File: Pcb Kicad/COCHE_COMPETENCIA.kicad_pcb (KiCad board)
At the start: 2 copper layers, 95 x 62 mm, 29 parts, among them J1 BAT, J2 SWITCH, J4 M1, J5 M2, J6 SENSORES, SW1 SW_Push, SW2 SW_Push, U1 L7805, U2 ESP32-DEVKIT-V1, U3 DRV8833, U4 DRV8833

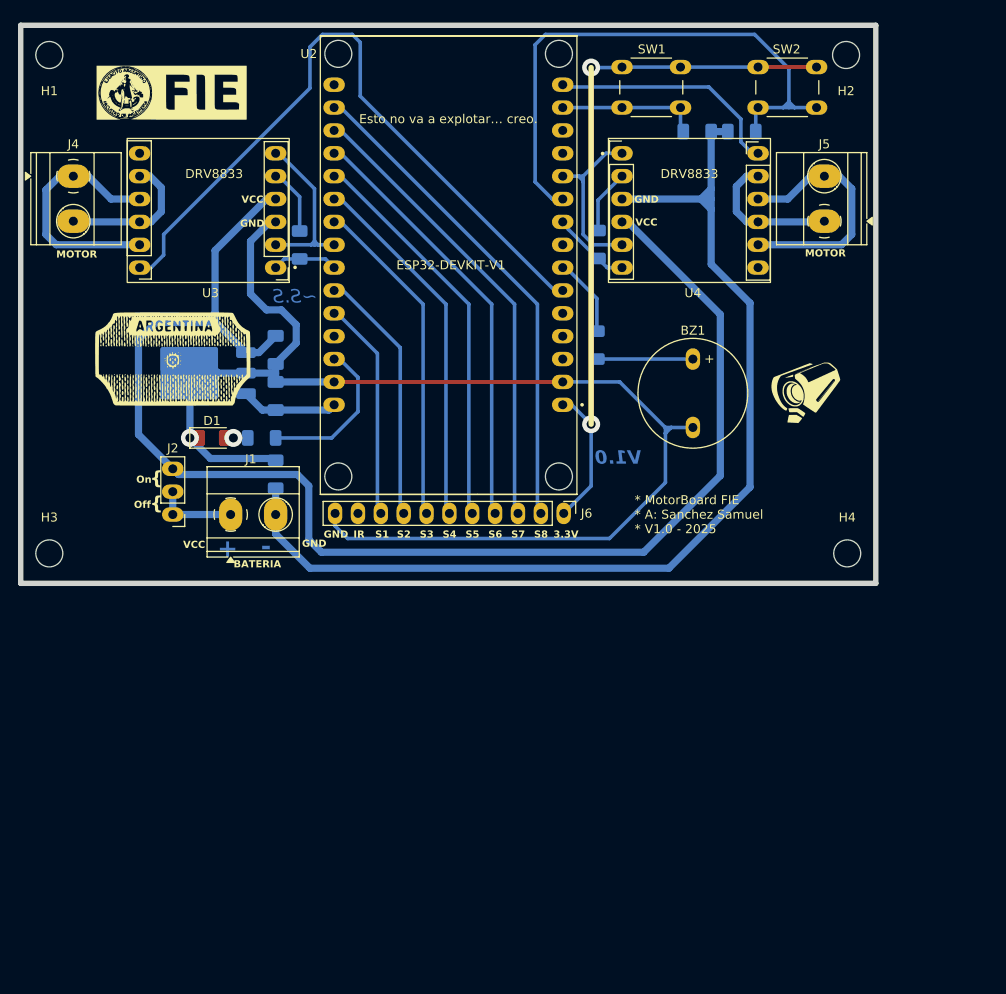
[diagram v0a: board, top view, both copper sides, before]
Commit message: V1.1 - Correccion de bocina y programas de motores.
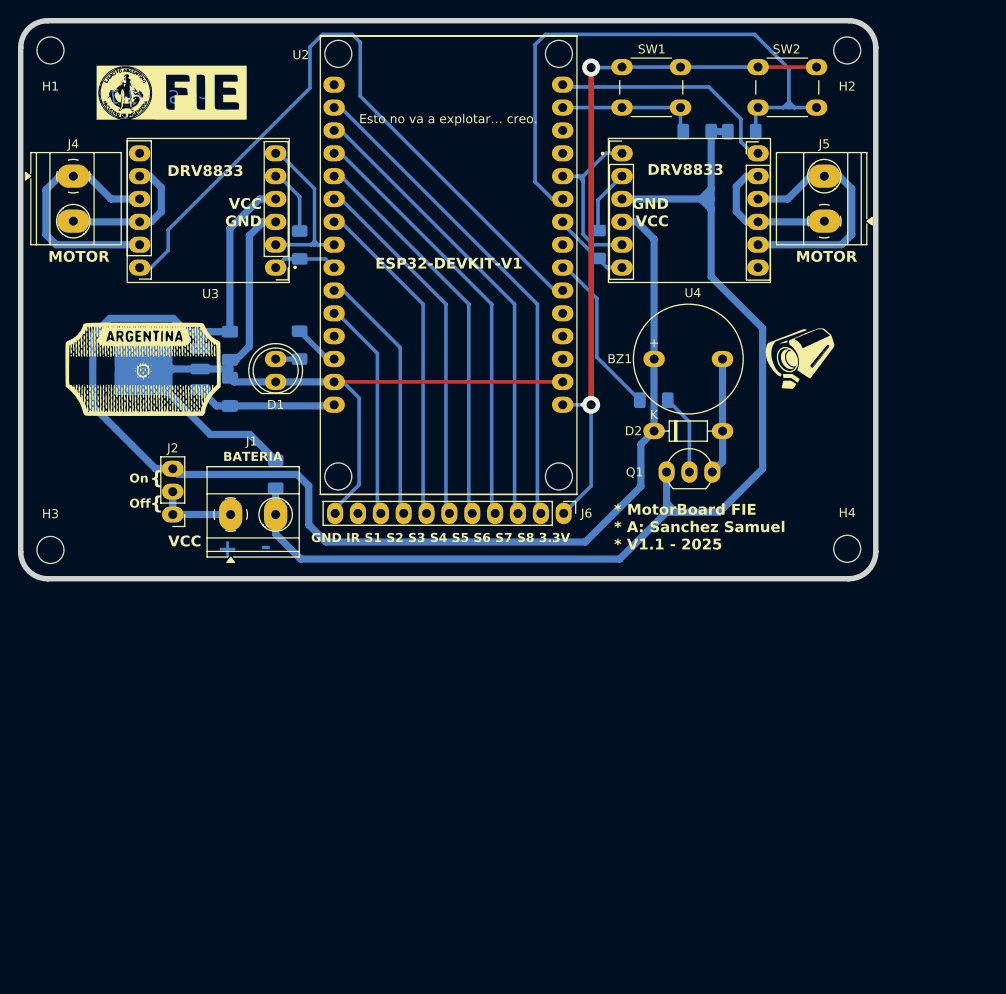
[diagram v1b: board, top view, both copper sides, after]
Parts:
- added D2: 1N4148, Diode_THT:D_DO-35_SOD27_P7.62mm_Horizontal, F.Cu at (168.0, 69.8)
- added Q1: 2N3904, Package_TO_SOT_THT:TO-92_Inline_Wide, F.Cu at (169.4, 74.4)
- D1: footprint LED_SMD:LED_1206_3216Metric_Pad1.42x1.75mm_HandSolder -> LED_THT:LED_D5.0mm
- R7: value 0 -> 1k
- moved R4 11.1 mm to (128.7, 60.3), turned to -90 degrees
- moved D1 9.42 mm to (126.0, 64.4), turned to 90 degrees
- moved R7 8.80 mm to (168.0, 66.4), turned to 0 degrees
- moved C1 5.10 mm to (120.9, 60.4)
- moved C2 5.10 mm to (120.9, 65.5)
- moved U1 5.10 mm to (112.6, 63.0)
- moved BZ1 4.31 mm to (168.0, 61.8), turned to 0 degrees
- moved G*** 3.85 mm to (184.2, 61.8)
- moved G*** 3.49 mm to (111.3, 63.0)
- moved H1 0.52 mm to (101.0, 27.6)
- moved H2 0.52 mm to (189.5, 27.6)
- moved H4 0.51 mm to (189.5, 82.9)
- moved H3 0.40 mm to (101.0, 83.1)
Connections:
- BZ1 pad 1: Net-(BZ1-+) -> VCC
- BZ1 pad 2: GND -> Net-(BZ1--)
- R7 pad 2: Net-(BZ1-+) -> Net-(Q1-B)
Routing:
- net GND: track 269.8 -> 230.0 mm, vias 1 -> 0
- net Net-(BZ1--): track 0.00 -> 13.4 mm
- net /LED_LARGADA: track 17.7 -> 5.89 mm
- net Net-(BZ1-+): track 10.7 -> 0.00 mm
- net /BUZZER: track 8.85 -> 18.5 mm
- net Net-(Q1-B): track 0.00 -> 8.98 mm
- net VCC: track 157.4 -> 151.5 mm
- net +5V: track 10.8 -> 16.5 mm
- net +3.3V: track 80.6 -> 79.7 mm
- net Net-(D1-A): track 2.49 -> 2.67 mm, vias 1 -> 0
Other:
- outline, holes or cut-outs redrawn
- board text added: "* MotorBoard FIE * A: Sanchez Samuel * V1.1 - 2025"
- board text added: "GND IR S1 S2 S3 S4 S5 S6 S7 S8 3.3V"
- board text added: "GND VCC"
- board text added: "VCC GND"
- board text added: "~S.S - V1.1"
- board text removed: "* MotorBoard FIE * A: Sanchez Samuel * V1.0 - 2025"
- board text removed: "3.3V"
- board text removed: "GND"
- board text removed: "IR"
- board text removed: "S1"
- board text removed: "S2"
- board text removed: "S3"
- board text removed: "S4"
- board text removed: "S5"
- board text removed: "S6"
- board text removed: "S7"
- board text removed: "S8"
- board text removed: "V1.0"
- board text removed: "~S.S"

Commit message: V1.1 - Programa de Buzzer + Modulo Drv8833
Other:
- board text added: "ANTENA"
- board text added: "USB"
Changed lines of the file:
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@@
+		)
+	)
+	(gr_text "ANTENA"
+		(at 150.241 30.607 0)
+		(layer "F.SilkS")
+		(effects
+			(font
+				(size 2 2)
+				(thickness 0.45)
+				(bold yes)
+			)
+			(justify right bottom)
+		)
+	)
+	(gr_text "USB"
+		(at 147.193 72.39 0)
+		(layer "F.SilkS")
+		(effects
+			(font
+				(size 1.5 1.5)
+				(thickness 0.375)
+				(bold yes)
+			)
+			(justify right bottom)
 		)
 	)

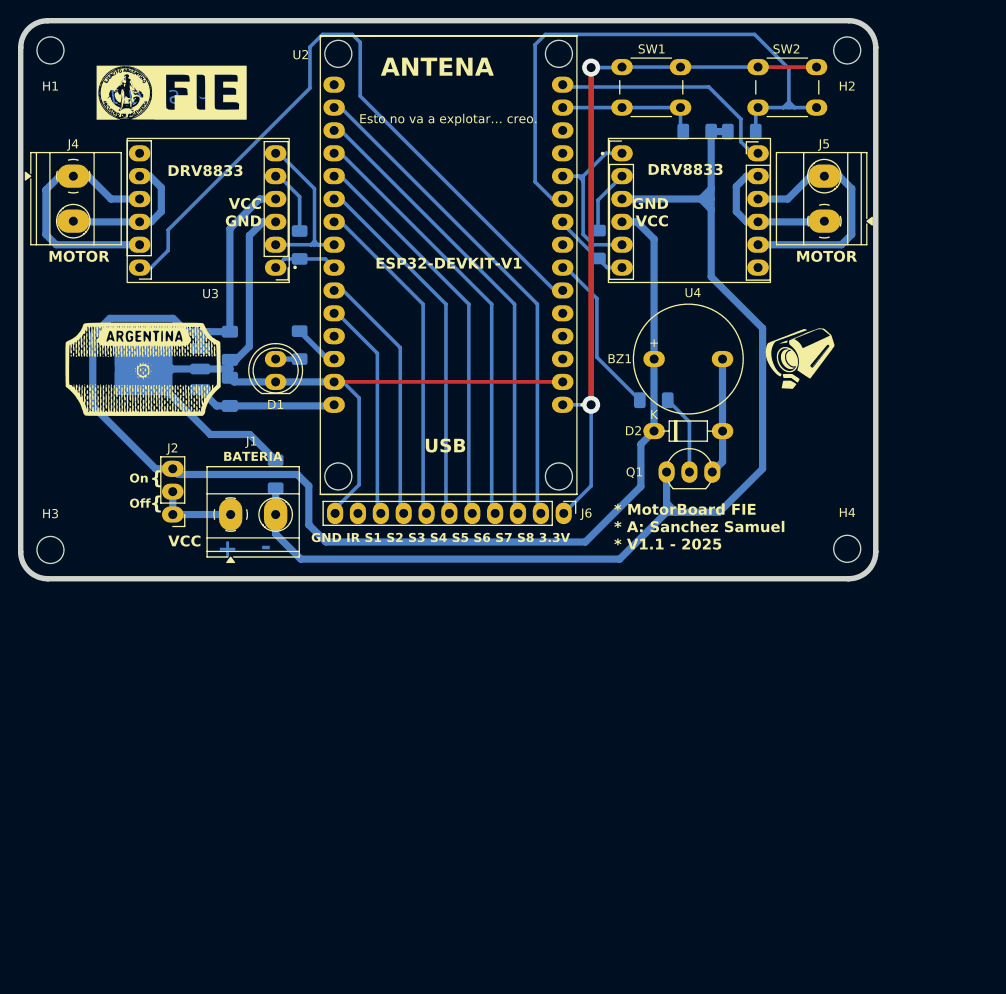
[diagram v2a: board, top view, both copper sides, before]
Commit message: V1.2 - Mejoras de PCB: alimentacion, bocina y borneras.
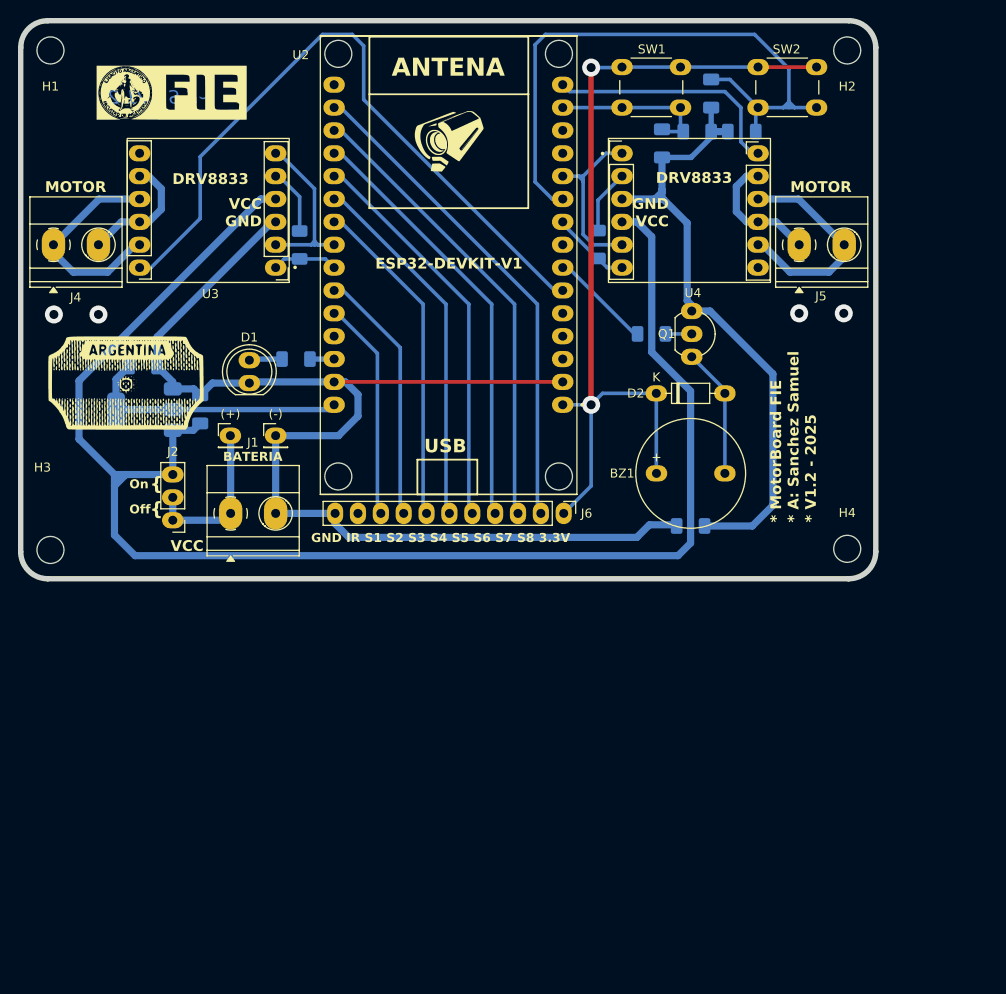
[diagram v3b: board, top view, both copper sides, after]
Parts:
- removed U1: L7805, Package_TO_SOT_SMD:TO-252-3_TabPin2
- added (+): TestPoint, Connector_PinHeader_2.54mm:PinHeader_1x01_P2.54mm_Vertical, F.Cu at (121.0, 70.4)
- added (-): TestPoint, Connector_PinHeader_2.54mm:PinHeader_1x01_P2.54mm_Vertical, F.Cu at (126.0, 70.4)
- added C3: 0.1u, Capacitor_SMD:C_1206_3216Metric_Pad1.33x1.80mm_HandSolder, B.Cu at (168.9, 37.9)
- added C4: 0.1u, Capacitor_SMD:C_1206_3216Metric_Pad1.33x1.80mm_HandSolder, B.Cu at (174.4, 32.3)
- added U5: AMS1117, Package_TO_SOT_SMD:SOT-223-3_TabPin2, B.Cu at (111.4, 67.5)
- moved R1 46.5 mm to (172.1, 80.4), turned to 180 degrees
- moved G*** 45.9 mm to (145.2, 37.7)
- moved Q1 18.1 mm to (172.2, 56.5), turned to -90 degrees
- moved BZ1 12.7 mm to (168.3, 74.5)
- moved C2 10.1 mm to (111.3, 62.6), turned to 0 degrees
- moved J4 7.93 mm to (101.3, 49.1), turned to 0 degrees
- moved C1 7.80 mm to (117.6, 67.4), turned to 90 degrees
- moved R7 7.37 mm to (167.7, 59.1)
- moved D2 4.20 mm to (168.3, 65.7)
- moved J5 3.83 mm to (184.2, 49.1), turned to 0 degrees
- moved D1 2.92 mm to (123.1, 64.5)
- moved G*** 2.44 mm to (109.3, 64.5)
- moved R4 1.60 mm to (128.2, 61.8), turned to 180 degrees
- moved J2 0.64 mm to (114.6, 79.8)
- moved J1 0.13 mm to (121.0, 79.0)
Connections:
- BZ1 pad 1: VCC -> +3.3V
- D2 pad 1: VCC -> +3.3V
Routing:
- net VCC: track 151.5 -> 170.9 mm
- net GND: track 230.0 -> 211.7 mm
- net +3.3V: track 79.7 -> 96.4 mm
- net +5V: track 16.5 -> 30.0 mm
- net Net-(J1-Pin_1): track 9.43 -> 18.8 mm
- net /SW2: track 64.7 -> 71.2 mm
- net Net-(Q1-B): track 8.98 -> 2.92 mm
- net /BUZZER: track 18.5 -> 12.6 mm
- net Net-(J4-Pin_1): track 27.9 -> 24.3 mm
- net Net-(J5-Pin_2): track 28.0 -> 24.6 mm
- net /LED_LARGADA: track 5.89 -> 2.68 mm
- net /SW1: track 15.9 -> 18.3 mm
- net Net-(J4-Pin_2): track 15.9 -> 13.9 mm
- net Net-(J5-Pin_1): track 16.0 -> 14.2 mm
- net Net-(BZ1--): track 13.4 -> 14.5 mm
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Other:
- board text added: "* MotorBoard FIE * A: Sanchez Samuel * V1.2 - 2025"
- board text added: "~S.S - V1.2"
- board text removed: "* MotorBoard FIE * A: Sanchez Samuel * V1.1 - 2025"
- board text removed: "+"
- board text removed: "-"
- board text removed: "Esto no va a explotar… creo."
- board text removed: "~S.S - V1.1"

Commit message: V1.3 - Diodo de proteccion + Mejor ubicacion de Sw's
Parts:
- added D3: 1N4148, Diode_THT:D_DO-35_SOD27_P7.62mm_Horizontal, F.Cu at (108.1, 82.3)
- moved C4 6.69 mm to (174.0, 39.0)
- moved R2 5.73 mm to (167.6, 39.0), turned to -90 degrees
- moved SW1 5.03 mm to (164.5, 34.4), turned to 90 degrees
- moved R3 2.86 mm to (176.3, 39.0), turned to -90 degrees
- moved C3 1.53 mm to (169.9, 39.0)
- moved SW2 1.50 mm to (179.5, 27.9), turned to -90 degrees
- renumbered (+) to (+)1, (-) to (-)1
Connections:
- J2 pad 3: VCC -> Net-(D3-A)
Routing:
- net /SW2: track 71.2 -> 53.0 mm
- net +3.3V: track 96.4 -> 108.0 mm
- net /SW1: track 18.3 -> 25.3 mm
- net Net-(D3-A): track 0.00 -> 6.48 mm
- net GND: track 211.7 -> 206.1 mm
- net /SLEEP_M2: track 27.1 -> 28.5 mm
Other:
- board text added: "* MotorBoard FIE * A: Sanchez Samuel * V1.3 - 2025"
- board text added: "2025 - V1.3"
- board text added: "~S.S"
- board text removed: "* MotorBoard FIE * A: Sanchez Samuel * V1.2 - 2025"
- board text removed: "~S.S - V1.2"

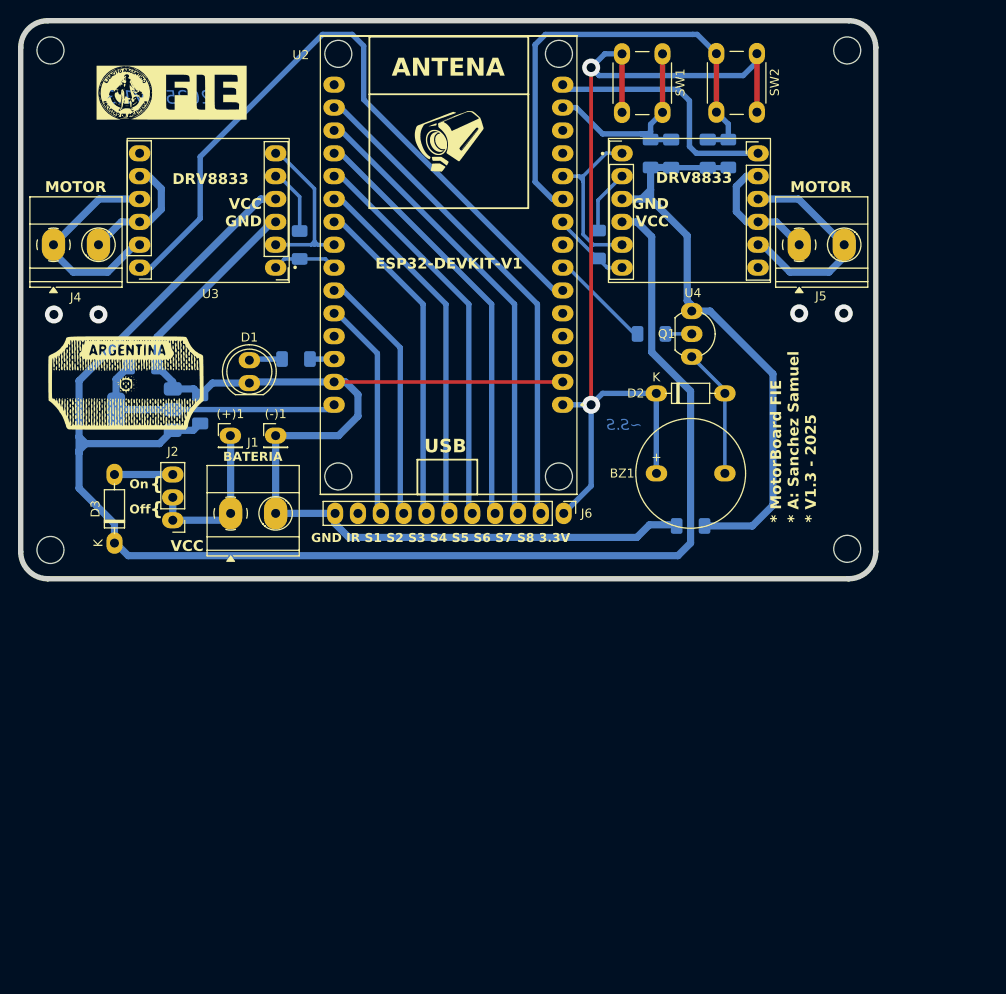
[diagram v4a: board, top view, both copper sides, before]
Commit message: V1.3 - Agregado de Prot. Tension inversa & pull downs y acomodado de componentes.
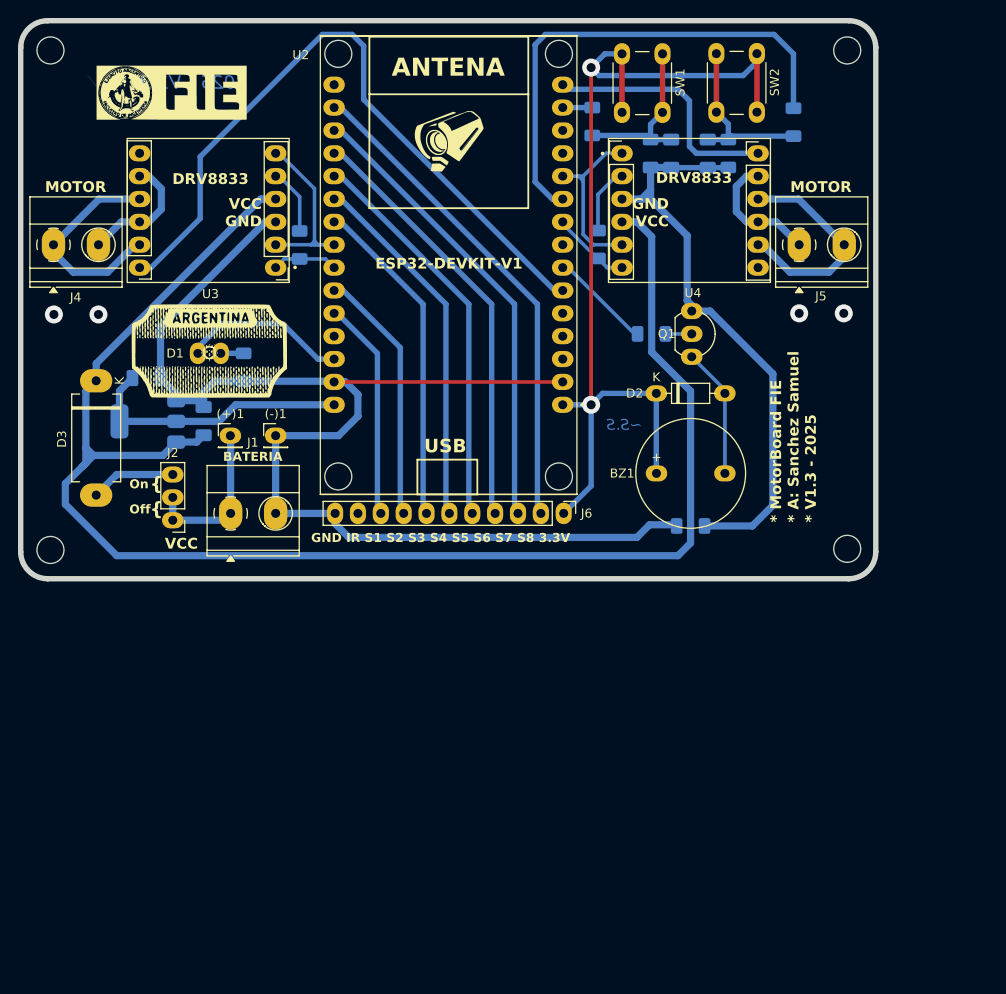
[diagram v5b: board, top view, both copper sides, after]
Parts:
- added G***: LOGO, LOGO, B.Cu at (108.3, 31.4)
- added R8: 100, Resistor_SMD:R_1206_3216Metric_Pad1.30x1.75mm_HandSolder, B.Cu at (183.5, 35.5)
- added R9: 100, Resistor_SMD:R_1206_3216Metric_Pad1.30x1.75mm_HandSolder, B.Cu at (161.2, 35.5)
- C1: value 0.33u -> 100n
- C2: value 0.1u -> 1u
- C3, C4: value 0.1u -> 100n
- D3: value 1N4148 -> 1N5822; footprint Diode_THT:D_DO-35_SOD27_P7.62mm_Horizontal -> Diode_THT:D_DO-201AD_P12.70mm_Horizontal
- moved D3 18.1 mm to (106.0, 64.3), turned to -90 degrees
- moved G*** 9.93 mm to (118.6, 61.0)
- moved R4 5.89 mm to (122.4, 62.8), turned to -90 degrees
- moved D1 4.58 mm to (119.9, 61.2), turned to 180 degrees
- moved C1 1.36 mm to (118.0, 68.7)
- moved C2 1.36 mm to (111.6, 64.0)
- moved U5 1.36 mm to (111.8, 68.8)
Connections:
- C3 pad 1: /SW1 -> Net-(C3-Pad1)
- C4 pad 1: /SW2 -> Net-(C4-Pad1)
- D1 pad 1: GND -> Net-(D1-K)
- D1 pad 2: Net-(D1-A) -> /LED_LARGADA
- R2 pad 1: /SW1 -> Net-(C3-Pad1)
- R3 pad 1: /SW2 -> Net-(C4-Pad1)
- R4 pad 1: /LED_LARGADA -> Net-(D1-K)
- R4 pad 2: Net-(D1-A) -> GND
- SW1 pad 2: /SW1 -> Net-(C3-Pad1)
- SW2 pad 2: /SW2 -> Net-(C4-Pad1)
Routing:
- net /SW1: track 25.3 -> 3.29 mm
- net Net-(C4-Pad1): track 0.00 -> 19.8 mm
- net Net-(C3-Pad1): track 0.00 -> 19.6 mm
- net /LED_LARGADA: track 2.68 -> 18.5 mm
- net Net-(D1-A): track 3.68 -> 0.00 mm
- net Net-(D3-A): track 6.48 -> 9.46 mm
- net GND: track 206.1 -> 208.9 mm
- net Net-(D1-K): track 0.00 -> 2.54 mm
- net /SW2: track 53.0 -> 55.2 mm
- net VCC: track 170.9 -> 172.8 mm
- net +5V: track 30.0 -> 30.9 mm
